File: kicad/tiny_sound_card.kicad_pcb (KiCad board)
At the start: 2 copper layers, 46 parts, among them CON1 BARREL_JACK, IC1 ATMEGA328P-A, J1 TRS_JACK, M1 DFR0299, P1 EXT_PWR, P2 SPKOUT, P3 EXT_SW0, P4 EXT_I2C, P4 M3Drill, P5 EXT_SW1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

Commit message: デザインルールを設定
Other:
- net class Default: trace_width 0.25 -> 0.2; via_dia 0.6 -> 0.7; via_drill 0.4 -> 0.3
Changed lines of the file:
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@@
   )
   (setup
-    (last_trace_width 0.25)
+    (last_trace_width 0.2)
     (trace_clearance 0.2)
     (zone_clearance 0.508)
@@
     (segment_width 0.2)
     (edge_width 0.15)
-    (via_size 0.6)
-    (via_drill 0.4)
+    (via_size 0.7)
+    (via_drill 0.3)
     (via_min_size 0.4)
     (via_min_drill 0.3)
@@
   (net_class Default "これは標準のネット クラスです。"
     (clearance 0.2)
-    (trace_width 0.25)
-    (via_dia 0.6)
-    (via_drill 0.4)
+    (trace_width 0.2)
+    (via_dia 0.7)
+    (via_drill 0.3)
     (uvia_dia 0.3)
     (uvia_drill 0.1)

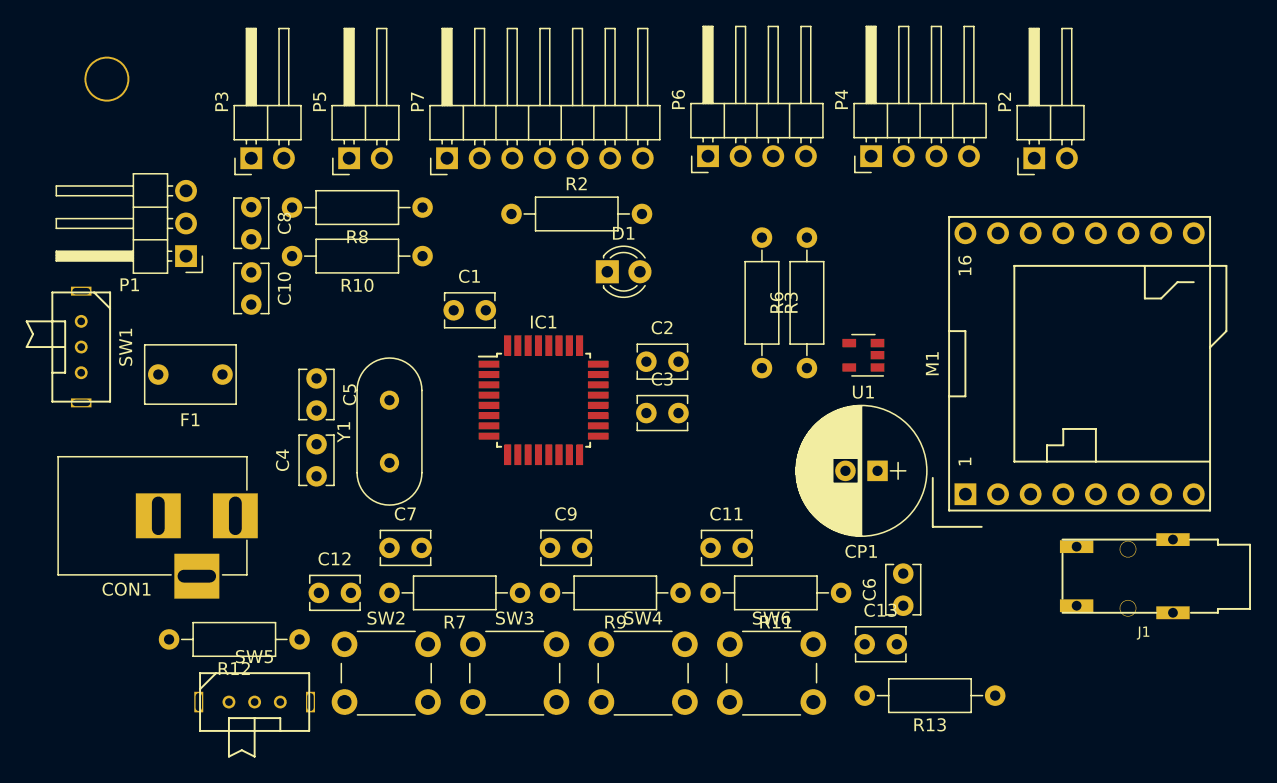
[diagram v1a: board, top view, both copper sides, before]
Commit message: GPIOのアサインを大幅に調整
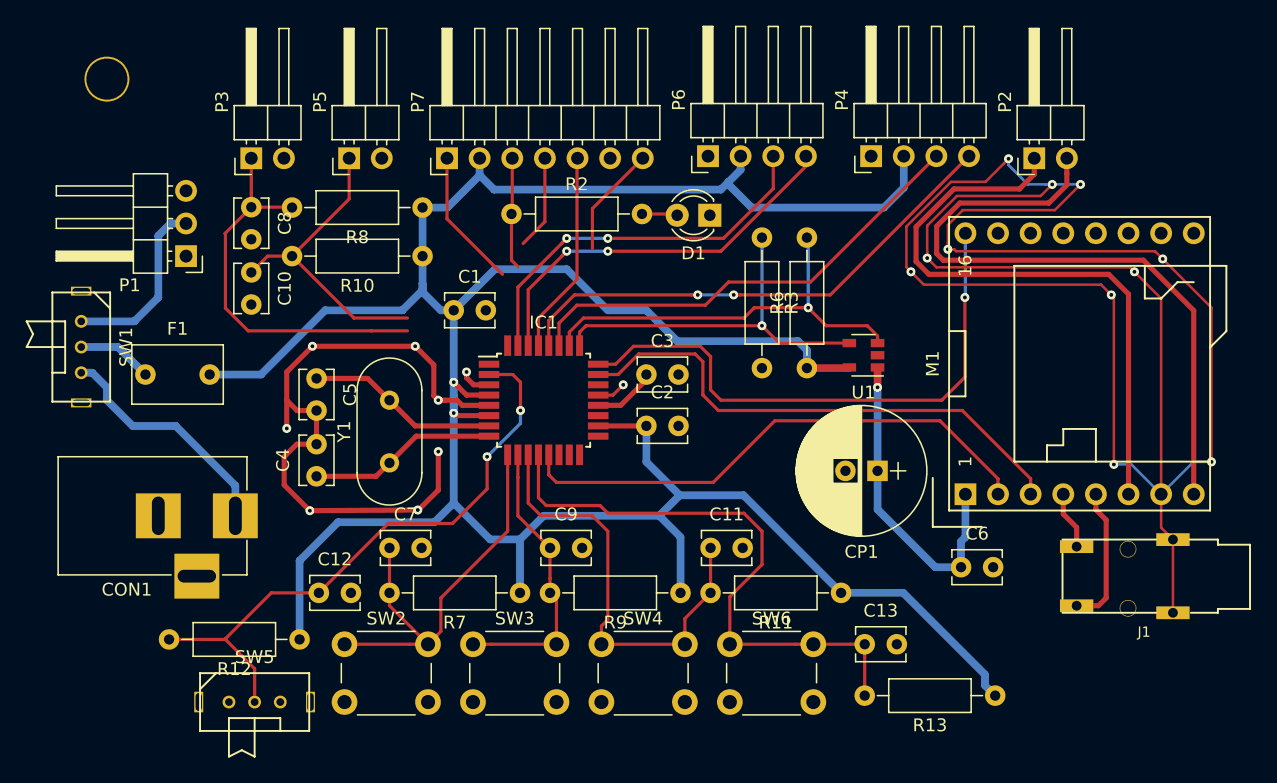
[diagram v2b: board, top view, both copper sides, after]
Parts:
- moved D1 9.11 mm to (101.9, 75.6), turned to 180 degrees
- moved F1 6.00 mm to (58.0, 88.0), turned to 0 degrees
- moved C6 5.41 mm to (121.5, 103.0), turned to 0 degrees
- moved C2 5.00 mm to (97.0, 92.0)
- moved C3 3.00 mm to (97.0, 88.0)
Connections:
- net Net-(C6-Pad1) renamed /DFR_VCC
- net Net-(CON1-Pad1) renamed /CONN_VCC
- net Net-(J1-Pad2) renamed /DAC_L
- net Net-(J1-Pad3) renamed /DAC_R
- net Net-(P1-Pad2) renamed /EXT_VCC
- C10 pad 1: /D7 -> /EXT_SW1
- C11 pad 1: /A2 -> /BTN2
- C12 pad 1: /D5 -> /D4
- C13 pad 1: /A3 -> /BTN3
- C7 pad 1: /A0 -> /BTN0
- C8 pad 1: /D6 -> /EXT_SW0
- C9 pad 1: /A1 -> /BTN1
- F1 pad 1: VCC -> /SEL_VCC
- F1 pad 2: Net-(F1-Pad2) -> VCC
- IC1 pad 1: /ATMEGA_RX -> /D3
- IC1 pad 10: /D6 -> /BTN1
- IC1 pad 11: /D7 -> /BTN2
- IC1 pad 12: /D8 -> /BTN3
- IC1 pad 13: /D9 -> /ATMEGA_TX
- IC1 pad 32: /ATMEGA_TX -> /D2
- IC1 pad 9: /D5 -> /BTN0
- M1 pad 16: /D4 -> /A1
- M1 pad 3: /ATMEGA_RX -> /A0
- M1 pad 6: Net-(M1-Pad6) -> /SPK2
- M1 pad 8: Net-(M1-Pad8) -> /SPK1
- P2 pad 1: Net-(M1-Pad8) -> /SPK2
- P2 pad 2: Net-(M1-Pad6) -> /SPK1
- P3 pad 1: /D6 -> /EXT_SW0
- P5 pad 1: /D7 -> /EXT_SW1
- R10 pad 2: /D7 -> /EXT_SW1
- R11 pad 2: /A2 -> /BTN2
- R12 pad 2: /D5 -> /D4
- R13 pad 2: /A3 -> /BTN3
- R3 pad 1: /D8 -> /A2
- R6 pad 2: /D9 -> /A3
- R7 pad 2: /A0 -> /BTN0
- R8 pad 2: /D6 -> /EXT_SW0
- R9 pad 2: /A1 -> /BTN1
- SW1 pad 2: Net-(F1-Pad2) -> /SEL_VCC
- SW2 pad 1: /A0 -> /BTN0
- SW3 pad 1: /A1 -> /BTN1
- SW4 pad 1: /A2 -> /BTN2
- SW5 pad 2: /D5 -> /D4
- SW6 pad 1: /A3 -> /BTN3
- U1 pad 3: /D9 -> /A3
- U1 pad 4: /D8 -> /A2
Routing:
- net VCC: track 0.00 -> 227.7 mm, vias 0 -> 2
- net GND: track 0.00 -> 221.6 mm, vias 0 -> 20
- net /SPK1: track 0.00 -> 51.8 mm
- net /SPK2: track 0.00 -> 48.0 mm
- net /D4: track 0.00 -> 47.5 mm, vias 0 -> 2
- net /BTN3: track 0.00 -> 46.2 mm
- net /A1: track 0.00 -> 44.4 mm, vias 0 -> 1
- net /ATMEGA_TX: track 0.00 -> 41.8 mm
- net /A0: track 0.00 -> 41.1 mm
- net /A5: track 0.00 -> 40.0 mm, vias 0 -> 2
- net /A4: track 0.00 -> 36.5 mm
- net /BTN2: track 0.00 -> 34.7 mm
- net /A3: track 0.00 -> 32.8 mm, vias 0 -> 1
- net /BTN0: track 0.00 -> 32.6 mm
- net /D0: track 0.00 -> 31.0 mm, vias 0 -> 2
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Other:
- net class Analog added: clearance 0.25, trace_width 0.4, via_dia 0.7, via_drill 0.3
- net class Default: trace_width 0.2 -> 0.25
- net class Power added: clearance 0.3, trace_width 0.6, via_dia 0.7, via_drill 0.3

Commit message: 基本配線終わり
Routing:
- net GND: track 221.6 -> 260.4 mm, vias 20 -> 28
- net /D10: track 8.66 -> 39.2 mm, vias 0 -> 4
- net /D11: track 7.34 -> 31.2 mm, vias 0 -> 2
- net /D12: track 10.8 -> 28.1 mm, vias 0 -> 2
- net /D13: track 8.67 -> 25.5 mm, vias 0 -> 2
- net VCC: track 227.7 -> 235.8 mm
- net /ATMEGA_TX: track 41.8 -> 43.2 mm
- net /BTN2: track 34.7 -> 33.6 mm

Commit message: 外形とパネル表裏を作成
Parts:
- added P10: M3Drill, kamiya:M3Drill2, F.Cu at (138.0, 112.0)
- added P8: M3Drill, kamiya:M3Drill2, F.Cu at (55.0, 112.0)
- added P9: M3Drill, kamiya:M3Drill2, F.Cu at (138.0, 65.0)
- moved SW1 2.15 mm to (53.2, 88.0)
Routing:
- net /CONN_VCC: track 18.6 -> 16.9 mm
- net /SEL_VCC: track 5.89 -> 4.80 mm
- net /EXT_VCC: track 14.1 -> 14.8 mm
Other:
- board outline added: 91 x 55 mm
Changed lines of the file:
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@@
     (links 118)
     (no_connects 51)
-    (area 28.000002 48.15 144.375001 119.825)
+    (area 50.924999 60.924999 142.075001 116.075001)
     (thickness 1.6)
-    (drawings 14)
-    (tracks 483)
+    (drawings 62)
+    (tracks 480)
     (zones 0)
-    (modules 46)
+    (modules 49)
     (nets 47)
   )
@@
     (38 B.Mask user)
     (39 F.Mask user)
-    (40 Dwgs.User user)
+    (40 Dwgs.User user hide)
     (41 Cmts.User user)
     (42 Eco1.User user)
@@
     (add_net VCC)
   )
+  (module kamiya:M3Drill2 locked (layer F.Cu)
+    (at 138 112)
+    (fp_text reference P10 (at 0 3) (layer F.SilkS) hide
+      (effects (font (size 1 1) (thickness 0.15)))
+    )
+    (fp_text value M3Drill (at 0 -3) (layer F.Fab) hide
+      (effects (font (size 1 1) (thickness 0.15)))
+    )
+    (pad "" np_thru_hole circle (at 0 0) (size 3.5 3.5) (drill 3.2) (layers *.Cu F.SilkS)
+      (clearance 0.2))
+  )
+  (module kamiya:M3Drill2 locked (layer F.Cu)
+    (at 138 65)
+    (fp_text reference P9 (at 0 3) (layer F.SilkS) hide
+      (effects (font (size 1 1) (thickness 0.15)))
+    )
+    (fp_text value M3Drill (at 0 -3) (layer F.Fab) hide
+      (effects (font (size 1 1) (thickness 0.15)))
+    )
+    (pad "" np_thru_hole circle (at 0 0) (size 3.5 3.5) (drill 3.2) (layers *.Cu F.SilkS)
+      (clearance 0.2))
+  )
+  (module kamiya:M3Drill2 locked (layer F.Cu)
+    (at 55 112)
+    (fp_text reference P8 (at 0 3) (layer F.SilkS) hide
+      (effects (font (size 1 1) (thickness 0.15)))
+    )
+    (fp_text value M3Drill (at 0 -3) (layer F.Fab) hide
+      (effects (font (size 1 1) (thickness 0.15)))
+    )
+    (pad "" np_thru_hole circle (at 0 0) (size 3.5 3.5) (drill 3.2) (layers *.Cu F.SilkS)
+      (clearance 0.2))
+  )
   (module Capacitors_ThroughHole:C_Disc_D3.8mm_W2.6mm_P2.50mm (layer F.Cu)
     (at 82 83)
@@
   )
   (module kamiya:SK-12D01-VG4 (layer F.Cu)
-    (at 53 85.86 270)
+    (at 53.2 88 270)
     (descr http://akizukidenshi.com/catalog/g/gP-08789/)
     (tags SW)
@@
     )
   )
+  (gr_line (start 140 116) (end 53 116) (layer Eco2.User) (width 0.2))
+  (gr_line (start 142 63) (end 142 114) (layer Eco2.User) (width 0.2))
+  (gr_line (start 53 61) (end 140 61) (layer Eco2.User) (width 0.2))
+  (gr_line (start 51 114) (end 51 63) (layer Eco2.User) (width 0.2))
+  (gr_arc (start 53 114) (end 53 116) (angle 90) (layer Eco2.User) (width 0.2))
+  (gr_arc (start 140 114) (end 142 114) (angle 90) (layer Eco2.User) (width 0.2))
+  (gr_arc (start 140 63) (end 140 61) (angle 90) (layer Eco2.User) (width 0.2))
+  (gr_arc (start 53 63) (end 51 63) (angle 90) (layer Eco2.User) (width 0.2))
+  (gr_line (start 51 114) (end 51 63) (layer Eco1.User) (width 0.2))
+  (gr_line (start 70 116) (end 53 116) (layer Eco1.User) (width 0.2))
+  (gr_line (start 72 108) (end 72 114) (layer Eco1.User) (width 0.2))
+  (gr_line (start 110 106) (end 74 106) (layer Eco1.User) (width 0.2))
+  (gr_line (start 112 114) (end 112 108) (layer Eco1.User) (width 0.2))
+  (gr_line (start 140 116) (end 114 116) (layer Eco1.User) (width 0.2))
+  (gr_line (start 142 63) (end 142 114) (layer Eco1.User) (width 0.2))
+  (gr_line (start 53 61) (end 140 61) (layer Eco1.User) (width 0.2))
+  (gr_arc (start 53 114) (end 53 116) (angle 90) (layer Eco1.User) (width 0.2))
+  (gr_arc (start 70 114) (end 72 114) (angle 90) (layer Eco1.User) (width 0.2))
+  (gr_arc (start 74 108) (end 72 108) (angle 90) (layer Eco1.User) (width 0.2))
+  (gr_arc (start 110 108) (end 110 106) (angle 90) (layer Eco1.User) (width 0.2))
+  (gr_arc (start 114 114) (end 114 116) (angle 90) (layer Eco1.User) (width 0.2))
+  (gr_arc (start 140 114) (end 142 114) (angle 90) (layer Eco1.User) (width 0.2))
+  (gr_arc (start 140 63) (end 140 61) (angle 90) (layer Eco1.User) (width 0.2))
+  (gr_arc (start 53 63) (end 51 63) (angle 90) (layer Eco1.User) (width 0.2))
+  (gr_line (start 51 69) (end 51 63) (layer Edge.Cuts) (width 0.15))
+  (gr_line (start 55 71) (end 53 71) (layer Edge.Cuts) (width 0.15))
+  (gr_line (start 57 80) (end 57 73) (layer Edge.Cuts) (width 0.15))
+  (gr_arc (start 53 69) (end 53 71) (angle 90) (layer Edge.Cuts) (width 0.15))
+  (gr_arc (start 55 73) (end 55 71) (angle 90) (layer Edge.Cuts) (width 0.15))
+  (gr_line (start 53 82) (end 55 82) (layer Edge.Cuts) (width 0.15))
+  (gr_line (start 51 114) (end 51 84) (layer Edge.Cuts) (width 0.15))
+  (gr_line (start 140 116) (end 53 116) (layer Edge.Cuts) (width 0.15))
+  (gr_line (start 142 63) (end 142 114) (layer Edge.Cuts) (width 0.15))
+  (gr_line (start 135 61) (end 140 61) (layer Edge.Cuts) (width 0.15))
+  (gr_line (start 133 65) (end 133 63) (layer Edge.Cuts) (width 0.15))
+  (gr_line (start 65 67) (end 131 67) (layer Edge.Cuts) (width 0.15))
+  (gr_line (start 63 63) (end 63 65) (layer Edge.Cuts) (width 0.15))
+  (gr_line (start 61 61) (end 53 61) (layer Edge.Cuts) (width 0.15))
+  (gr_arc (start 53 84) (end 51 84) (angle 90) (layer Edge.Cuts) (width 0.15))
+  (gr_arc (start 55 80) (end 57 80) (angle 90) (layer Edge.Cuts) (width 0.15))
+  (gr_arc (start 53 114) (end 53 116) (angle 90) (layer Edge.Cuts) (width 0.15))
+  (gr_arc (start 140 114) (end 142 114) (angle 90) (layer Edge.Cuts) (width 0.15))
+  (gr_arc (start 140 63) (end 140 61) (angle 90) (layer Edge.Cuts) (width 0.15))
+  (gr_arc (start 135 63) (end 133 63) (angle 90) (layer Edge.Cuts) (width 0.15))
+  (gr_arc (start 65 65) (end 65 67) (angle 90) (layer Edge.Cuts) (width 0.15))
+  (gr_arc (start 131 65) (end 133 65) (angle 90) (layer Edge.Cuts) (width 0.15))
+  (gr_arc (start 61 63) (end 61 61) (angle 90) (layer Edge.Cuts) (width 0.15))
+  (gr_arc (start 53 63) (end 51 63) (angle 90) (layer Edge.Cuts) (width 0.15))
   (gr_line (start 134 108) (end 142 108) (layer Dwgs.User) (width 0.2))
   (gr_line (start 134 116) (end 134 108) (layer Dwgs.User) (width 0.2))
@@
   (segment (start 121.84 100.66) (end 121.84 97.32) (width 0.6) (layer B.Cu) (net 32))
   (segment (start 121.5 103) (end 121.5 101) (width 0.6) (layer B.Cu) (net 32))
-  (segment (start 55 89) (end 53.86 87.86) (width 0.6) (layer B.Cu) (net 33))
-  (segment (start 53.86 87.86) (end 53 87.86) (width 0.6) (layer B.Cu) (net 33))
-  (segment (start 55 90) (end 55 89) (width 0.6) (layer B.Cu) (net 33))
-  (segment (start 57 92) (end 55 90) (width 0.6) (layer B.Cu) (net 33))
-  (segment (start 60.35 92) (end 57 92) (width 0.6) (layer B.Cu) (net 33))
   (segment (start 65 99) (end 65 96.65) (width 0.6) (layer B.Cu) (net 33))
   (segment (start 65 96.65) (end 60.35 92) (width 0.6) (layer B.Cu) (net 33))
-  (segment (start 53 85.86) (end 55.86 85.86) (width 0.6) (layer B.Cu) (net 34))
-  (segment (start 55.86 85.86) (end 58 88) (width 0.6) (layer B.Cu) (net 34))
+  (segment (start 60.35 92) (end 56.4 92) (width 0.6) (layer B.Cu) (net 33))
+  (segment (start 56.4 92) (end 54.4 90) (width 0.6) (layer B.Cu) (net 33))
+  (segment (start 54.4 90) (end 53.2 90) (width 0.6) (layer B.Cu) (net 33))
+  (segment (start 53.2 88) (end 58 88) (width 0.6) (layer B.Cu) (net 34))
   (segment (start 61.16 76.24) (end 59.957919 76.24) (width 0.6) (layer B.Cu) (net 35))
   (segment (start 59.957919 76.24) (end 59 77.197919) (width 0.6) (layer B.Cu) (net 35))
   (segment (start 59 77.197919) (end 59 82) (width 0.6) (layer B.Cu) (net 35))
-  (segment (start 59 82) (end 57.14 83.86) (width 0.6) (layer B.Cu) (net 35))
-  (segment (start 57.14 83.86) (end 53 83.86) (width 0.6) (layer B.Cu) (net 35))
+  (segment (start 55 86) (end 53.2 86) (width 0.6) (layer B.Cu) (net 35))
+  (segment (start 59 82) (end 55 86) (width 0.6) (layer B.Cu) (net 35))
   (segment (start 132 97.32) (end 132 98.522081) (width 0.4) (layer F.Cu) (net 36))
   (segment (start 132 98.522081) (end 132.8 99.322081) (width 0.4) (layer F.Cu) (net 36))

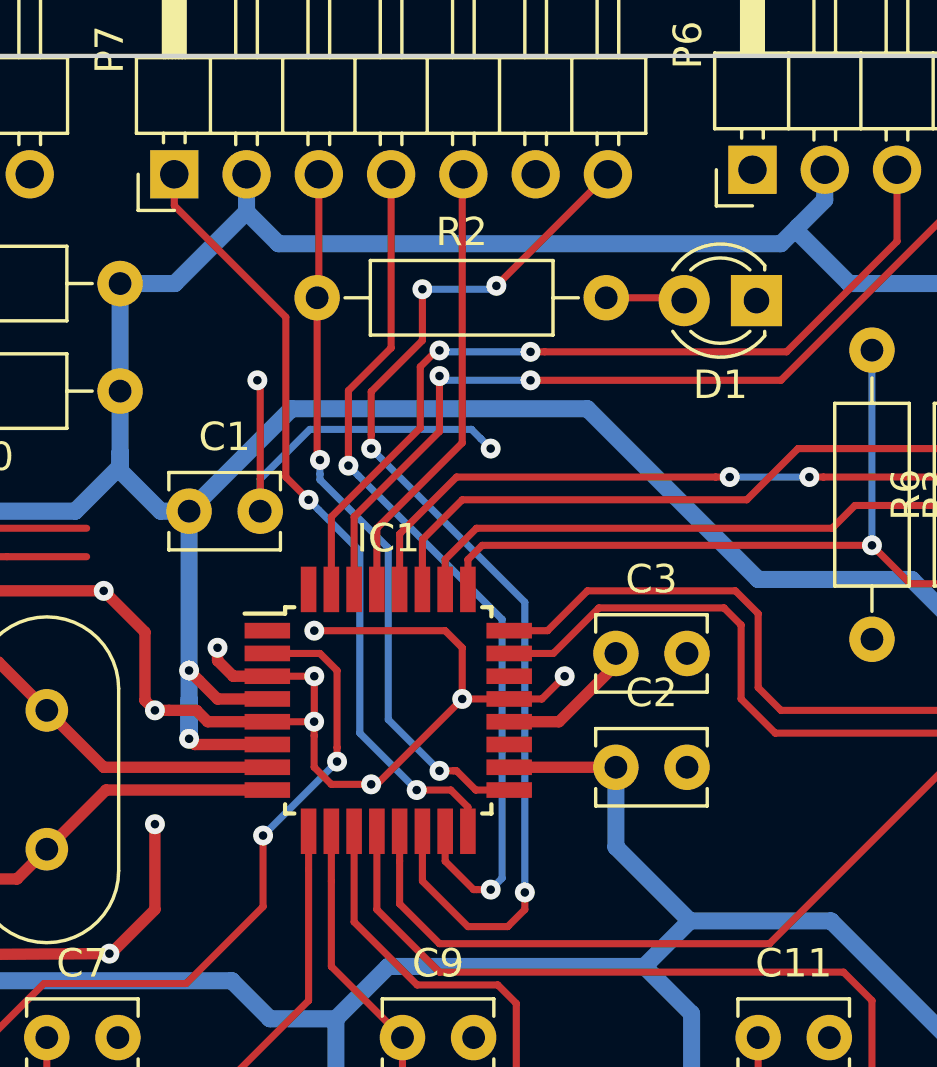
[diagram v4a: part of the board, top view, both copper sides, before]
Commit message: LEDのポートを変更
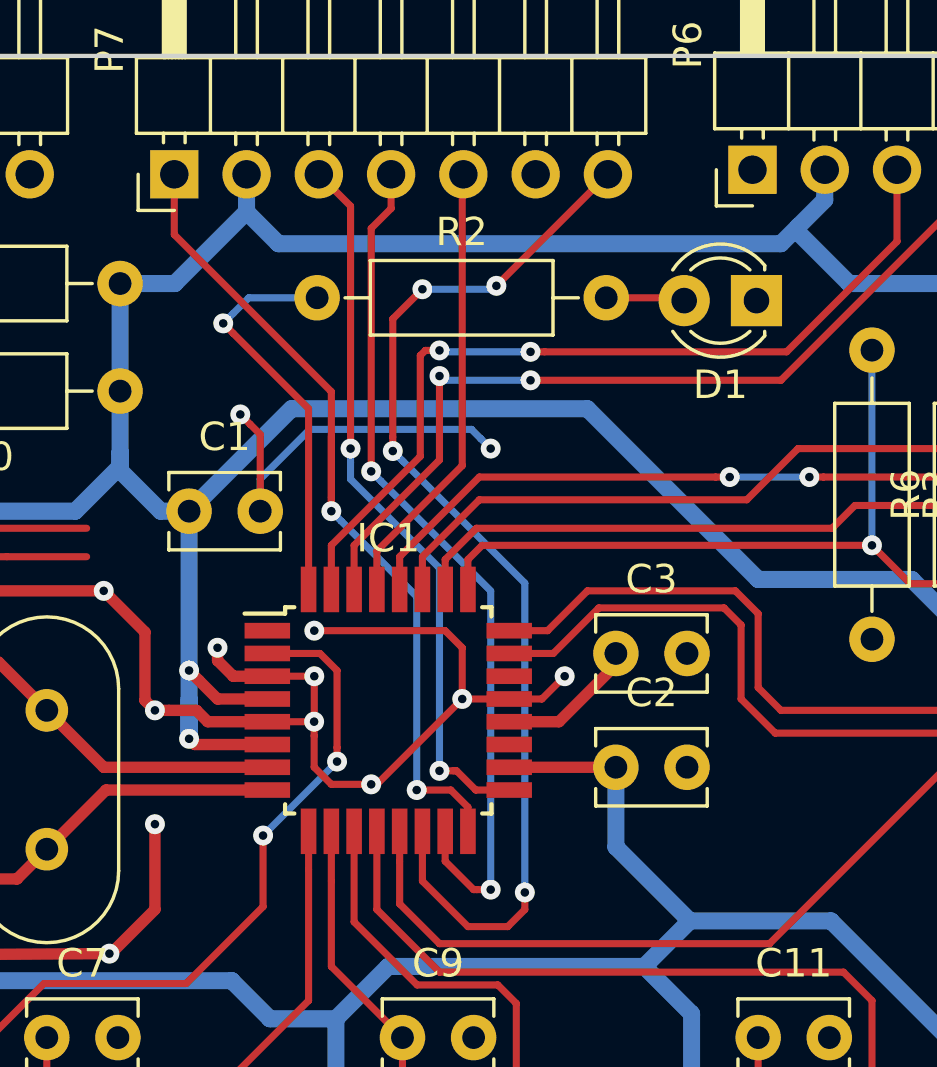
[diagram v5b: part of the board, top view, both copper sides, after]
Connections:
- R2 pad 1: /D13 -> /D2
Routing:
- net /D2: track 0.00 -> 14.4 mm, vias 0 -> 1
- net /D12: track 28.1 -> 30.7 mm
- net /D11: track 31.2 -> 30.2 mm
- net GND: track 260.4 -> 259.4 mm
- net /D10: track 39.2 -> 38.6 mm
